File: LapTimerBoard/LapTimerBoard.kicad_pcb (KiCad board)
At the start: 2 copper layers, 6 parts, among them J1 BLE-HM-10, J2 +5V, J3 GND, J4 RX5808_spi

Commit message: Updated PCB and generated first past of gerber file views.
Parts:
- removed A1: Arduino_Nano_v3.x, Module:Arduino_Nano
- removed BZ1: Buzzer, Buzzer_Beeper:MagneticBuzzer_Kingstate_KCG0601
- removed J1: BLE-HM-10, Connector_PinHeader_1.00mm:PinHeader_1x04_P1.00mm_Horizontal
- removed J2: +5V, Connector_PinHeader_1.00mm:PinHeader_1x02_P1.00mm_Horizontal
- removed J3: GND, Connector_PinHeader_1.00mm:PinHeader_1x02_P1.00mm_Horizontal
- removed J4: RX5808_spi, Connector_PinHeader_1.00mm:PinHeader_1x08_P1.00mm_Horizontal
- added +5V: +5V, Connector_PinHeader_2.54mm:PinHeader_1x02_P2.54mm_Vertical, F.Cu at (110.5, 121.9)
- added Arduino Nano V3: Arduino_Nano_v3.x, Module:Arduino_Nano, F.Cu at (119.7, 98.1)
- added BLE-HM-10: BLE-HM-10, Connector_PinHeader_2.54mm:PinHeader_1x04_P2.54mm_Vertical, F.Cu at (110.5, 138.4)
- added Buzzer: Buzzer, Buzzer_Beeper:Buzzer_15x7.5RM7.6, F.Cu at (109.2, 91.4)
- added GND: GND, Connector_PinHeader_2.54mm:PinHeader_1x02_P2.54mm_Vertical, F.Cu at (110.5, 110.5)
- added RX5808_spi: RX5808_spi, Connector_PinHeader_2.54mm:PinHeader_1x08_P2.54mm_Vertical, F.Cu at (118.1, 87.6)
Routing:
- net GND: track 0.00 -> 94.9 mm
- net VCC: track 0.00 -> 90.0 mm
- net Net-(A1-Pad1): track 0.00 -> 56.2 mm
- net Net-(A1-Pad2): track 0.00 -> 49.7 mm
- net /CH3: track 0.00 -> 48.5 mm
- net /CH2: track 0.00 -> 46.0 mm
- net /CH1: track 0.00 -> 43.4 mm
- net Net-(A1-Pad12): track 0.00 -> 40.7 mm
- net /RSSI: track 0.00 -> 39.5 mm

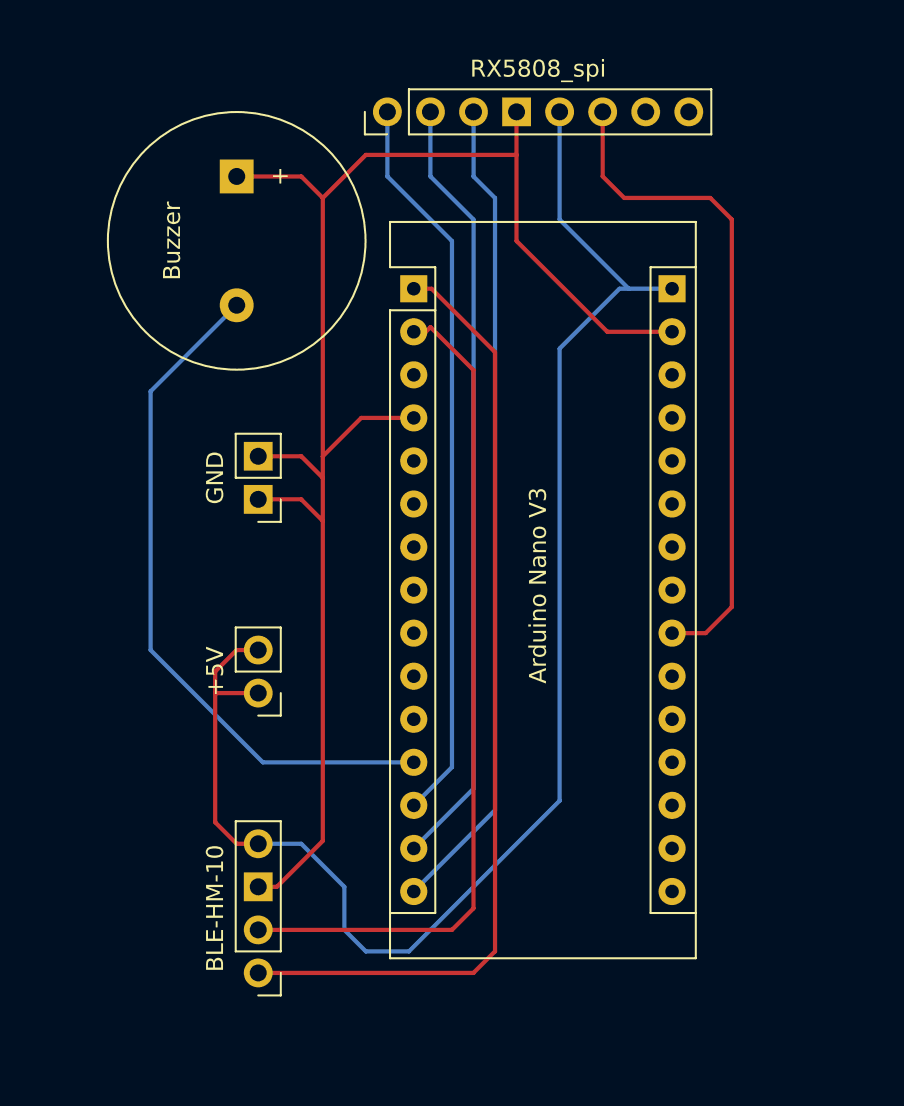
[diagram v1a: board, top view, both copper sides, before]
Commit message: updated with edge cuts and mounting holes
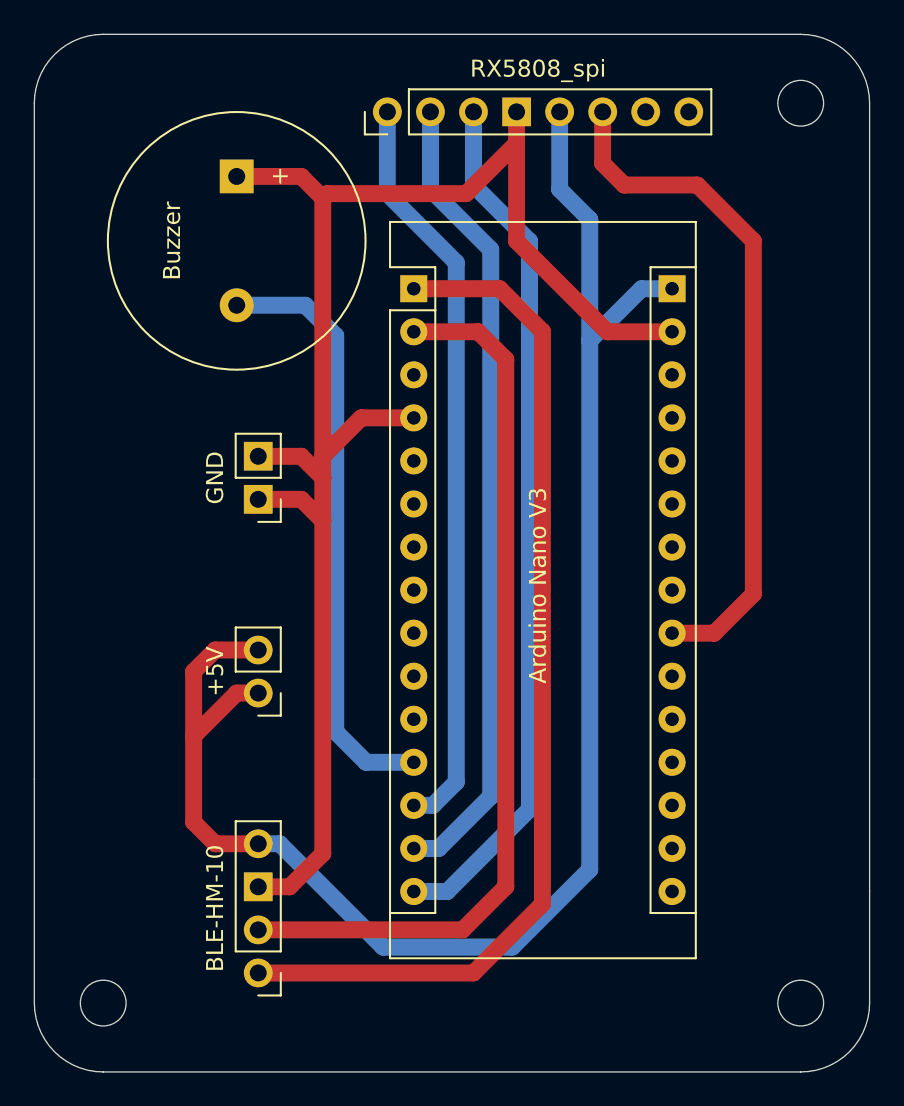
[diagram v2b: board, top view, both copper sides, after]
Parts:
- added REF**: MountingHole_2.7mm_M2.5, MountingHole:MountingHole_2.7mm_M2.5, F.Cu at (101.3, 140.2)
- added REF**: MountingHole_2.7mm_M2.5, MountingHole:MountingHole_2.7mm_M2.5, F.Cu at (142.5, 140.2)
- added REF**: MountingHole_2.7mm_M2.5, MountingHole:MountingHole_2.7mm_M2.5, F.Cu at (142.5, 87.1)
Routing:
- net VCC: track 90.0 -> 98.0 mm
- net Net-(A1-Pad12): track 40.7 -> 35.3 mm
- net Net-(A1-Pad1): track 56.2 -> 60.9 mm
- net Net-(A1-Pad2): track 49.7 -> 53.6 mm
- net /CH3: track 48.5 -> 51.4 mm
- net /CH2: track 46.0 -> 47.7 mm
- net /RSSI: track 39.5 -> 40.4 mm
- net /CH1: track 43.4 -> 44.3 mm
- net GND: track 94.9 -> 95.7 mm
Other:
- board outline added: 49.3 x 61.2 mm

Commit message: Gerber files generated and bearshampoo assets added into respective folder
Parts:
- added G***: LOGO, BearShampoo-Assests:BearShampoo-txt_300x300DPI, F.Cu at (103.1, 127.8)
- added G***: LOGO, BearShampoo-Assests:BearShampoo-Logo_800x800DPI, F.Cu at (103.0, 114.2)
- added REF**: OSHW-Logo2_9.8x8mm_SilkScreen, Symbol:OSHW-Logo2_9.8x8mm_SilkScreen, F.Cu at (141.1, 126.0)
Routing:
- added copper zone on B.Cu, net GND
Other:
- board text added: "Rev. 1.0"
